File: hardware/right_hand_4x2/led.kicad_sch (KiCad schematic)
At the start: 1 part

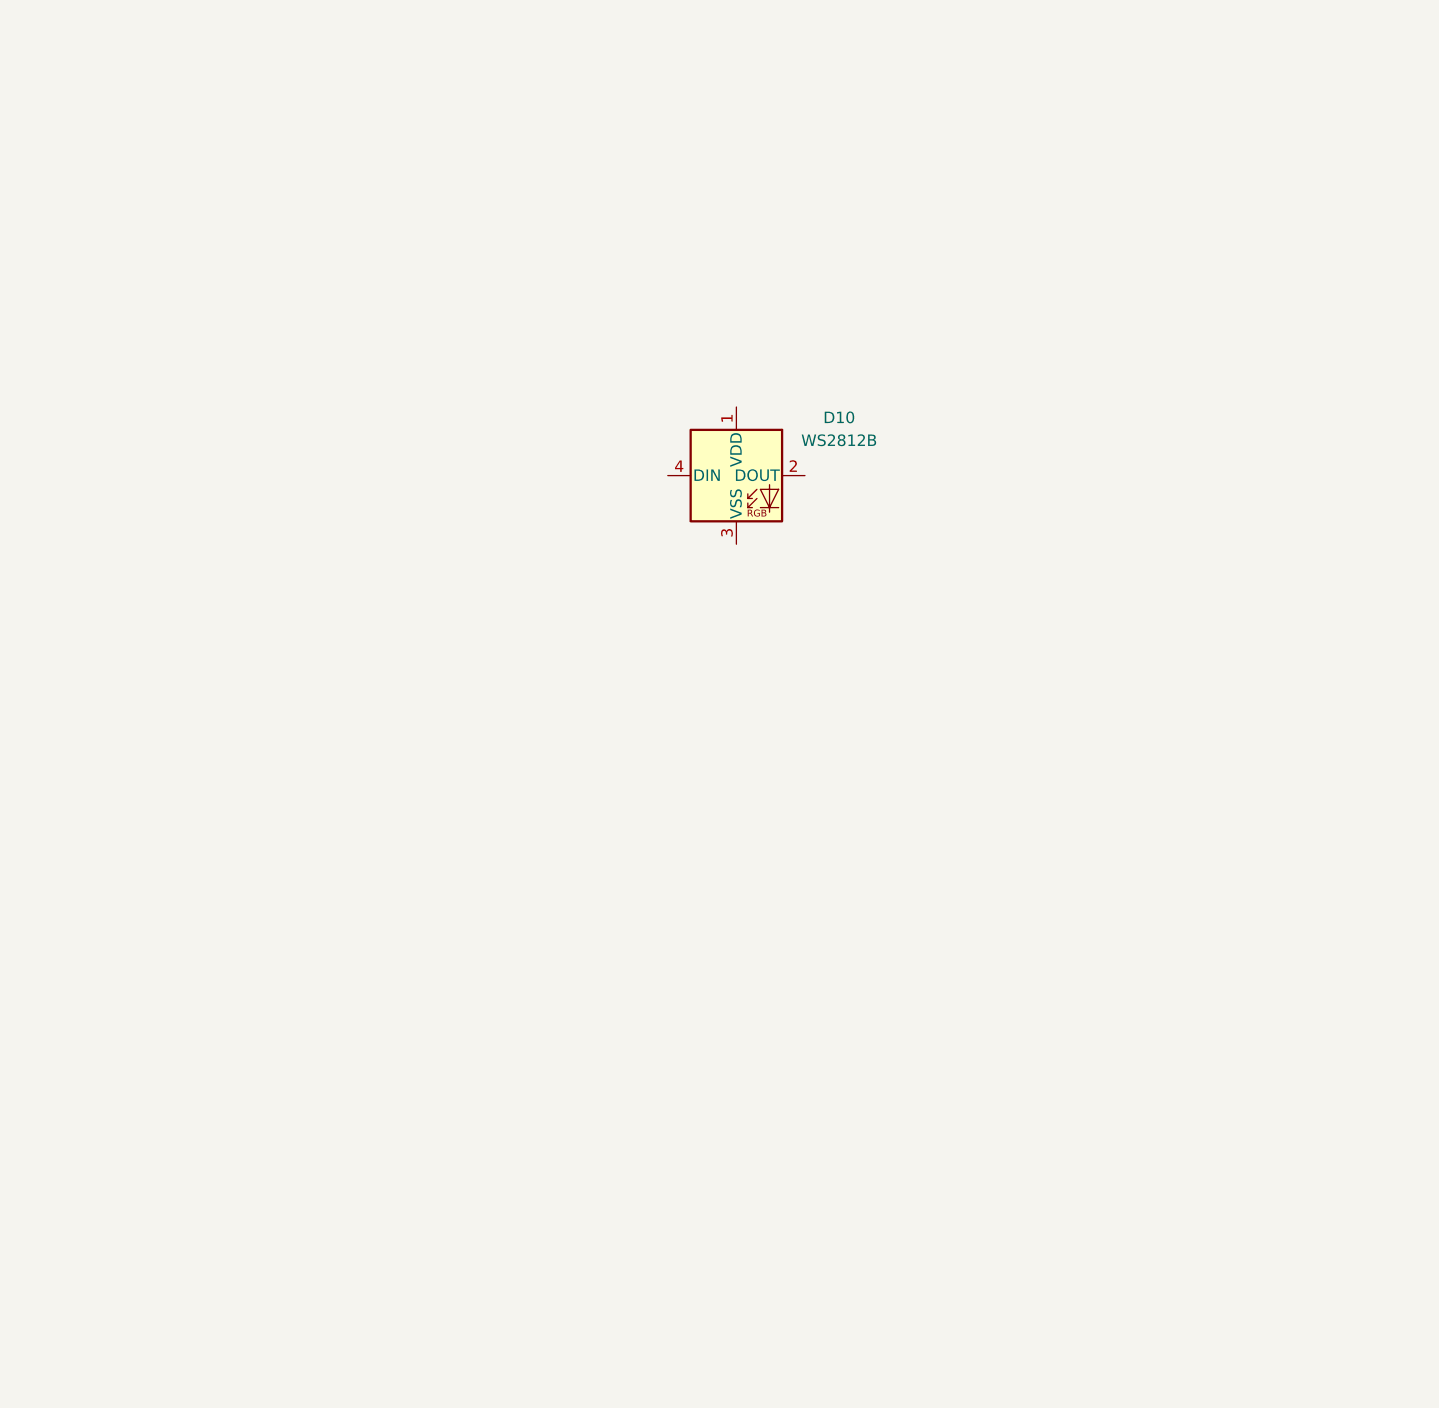
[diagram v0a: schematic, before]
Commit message: 4x2 schematic and layout update
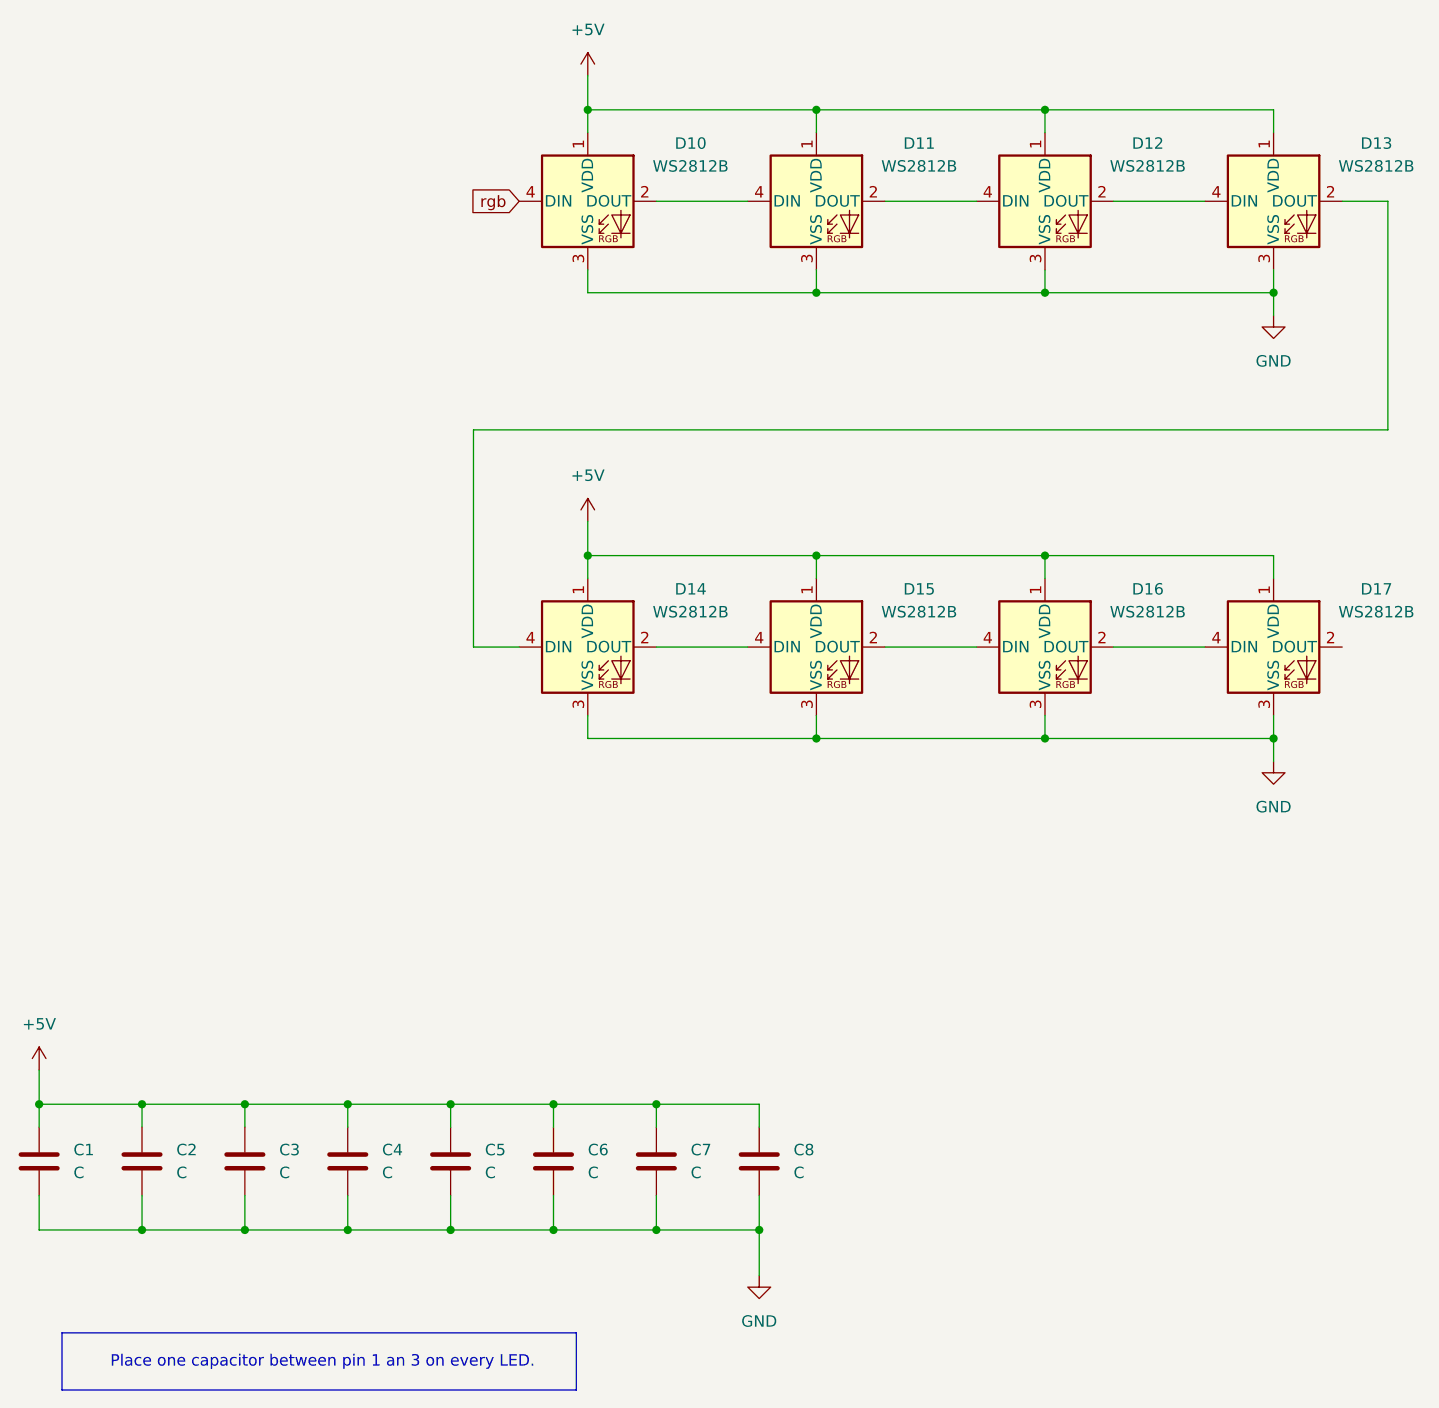
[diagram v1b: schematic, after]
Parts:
- added C1, C2, C3, C4, C5, C6, C7, C8: C, Capacitor_SMD:C_0805_2012Metric_Pad1.18x1.45mm_HandSolder, symbol Device:C
- added D11, D12, D13, D14, D15, D16, D17: WS2812B, LED_SMD:LED_WS2812B_PLCC4_5.0x5.0mm_P3.2mm, symbol LED:WS2812B
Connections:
- net +5V: now reaches D10.1 (VDD)
- net +5V: now also C1.1, C2.1, C3.1, C4.1, C5.1, C6.1, C7.1, C8.1, D11.1 (VDD), D12.1 (VDD), D13.1 (VDD), D14.1 (VDD), D15.1 (VDD), D16.1 (VDD), D17.1 (VDD)
- net at D10.2 (DOUT): now also D11.4 (DIN)
- net GND: now reaches D10.3 (VSS)
- net GND: now also C1.2, C2.2, C3.2, C4.2, C5.2, C6.2, C7.2, C8.2, D11.3 (VSS), D12.3 (VSS), D13.3 (VSS), D14.3 (VSS), D15.3 (VSS), D16.3 (VSS), D17.3 (VSS)
- net rgb: now reaches D10.4 (DIN)
- new net: D11.2 (DOUT), D12.4 (DIN)
- new net: D16.2 (DOUT), D17.4 (DIN)
- new net: D15.2 (DOUT), D16.4 (DIN)
- new net: D12.2 (DOUT), D13.4 (DIN)
- new net: D14.2 (DOUT), D15.4 (DIN)
- new net: D13.2 (DOUT), D14.4 (DIN)
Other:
- note added: "Place one capacitor between pin 1 an 3 on every LED."
- moved on the sheet: D10
